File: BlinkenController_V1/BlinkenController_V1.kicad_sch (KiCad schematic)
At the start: 45 parts, among them J1 Conn_01x02_Socket, J2 Conn_01x08_Socket, J4 Conn_01x03_Socket, J5 6P6C, J6 6P6C, J7 Conn_01x04_Pin, J8 Conn_01x06_Socket, SW1 SW_DIP_x01, SW2 SW_Push, SW3 SW_Push, SW4 SW_Push, SW5 SW_Push, SW6 SW_Push, U1 Pico, U2 MAX232, U3 TL331, U4 MAX3485, U5 TXS0108EPW

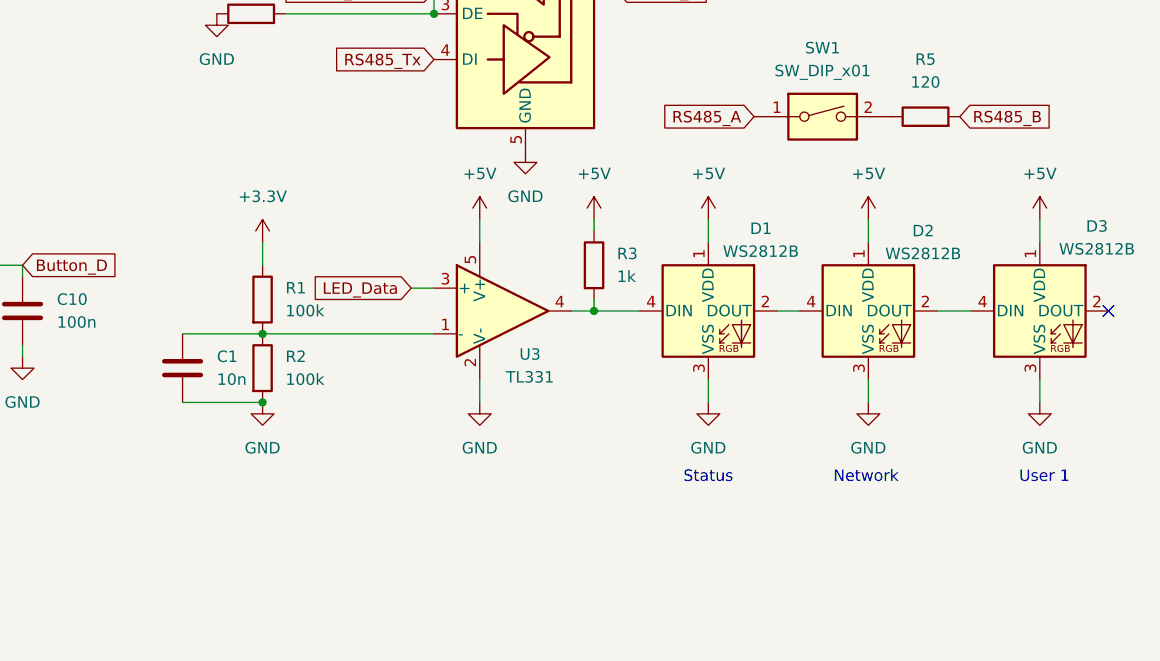
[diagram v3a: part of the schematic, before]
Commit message: Overhauled the output board
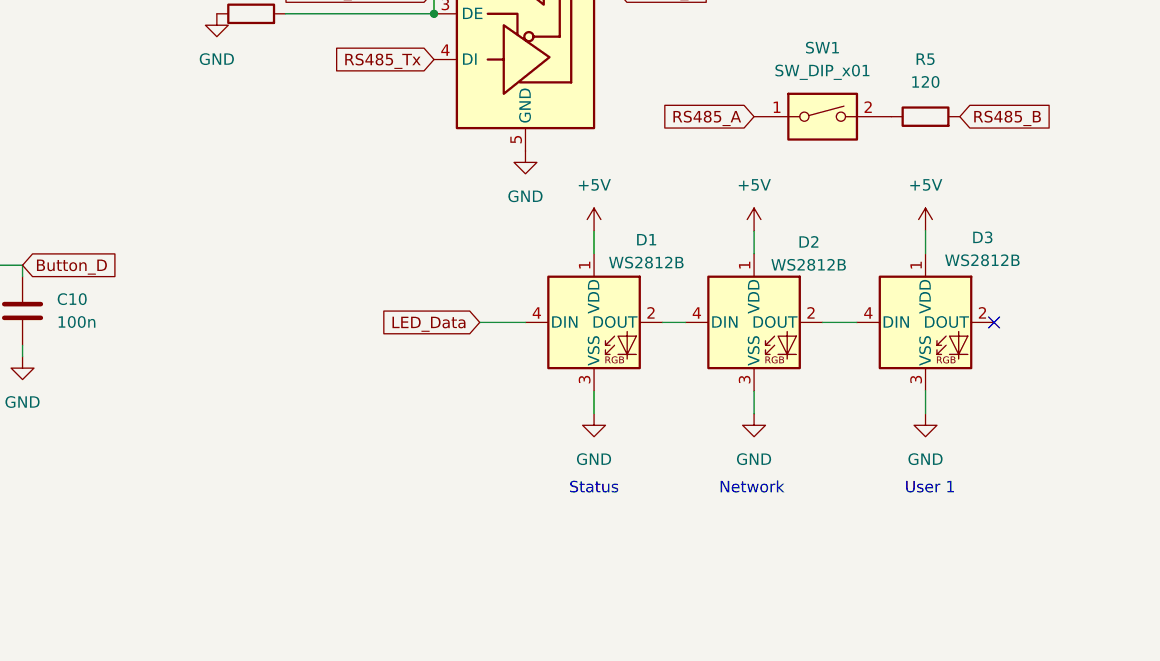
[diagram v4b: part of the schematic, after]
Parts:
- removed C1: 10n, Capacitor_SMD:C_0805_2012Metric_Pad1.18x1.45mm_HandSolder, symbol Device:C
- removed R1, R2: 100k, Resistor_SMD:R_0805_2012Metric_Pad1.20x1.40mm_HandSolder, symbol Device:R
- removed R3: 1k, Resistor_SMD:R_0805_2012Metric_Pad1.20x1.40mm_HandSolder, symbol Device:R
- removed U3: TL331, Package_TO_SOT_SMD:SOT-23-5, symbol Comparator:TL331
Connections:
- net LED_Data: now also D1.4 (DIN)
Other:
- moved on the sheet: D1, D2, D3
